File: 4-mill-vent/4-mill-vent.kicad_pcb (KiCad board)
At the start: 2 copper layers, 76.2 x 47.6 mm, 70 parts, among them J1 Fan, J2 Buzzer, J3 Power, J4 ICSP, Q3 PZT3904, Q4 PZT3904, Q5 TSM480P06CP, Q6 MMBT3904, SW1 Power_off, SW2 Power_On, SW3 Fan_Down, SW4 Fan_Up, U1 LM321, U2 ATmega328P-AU, U3 TPSM84212EAB, U4 LM1117-5.0, Y1 16.000MHZ

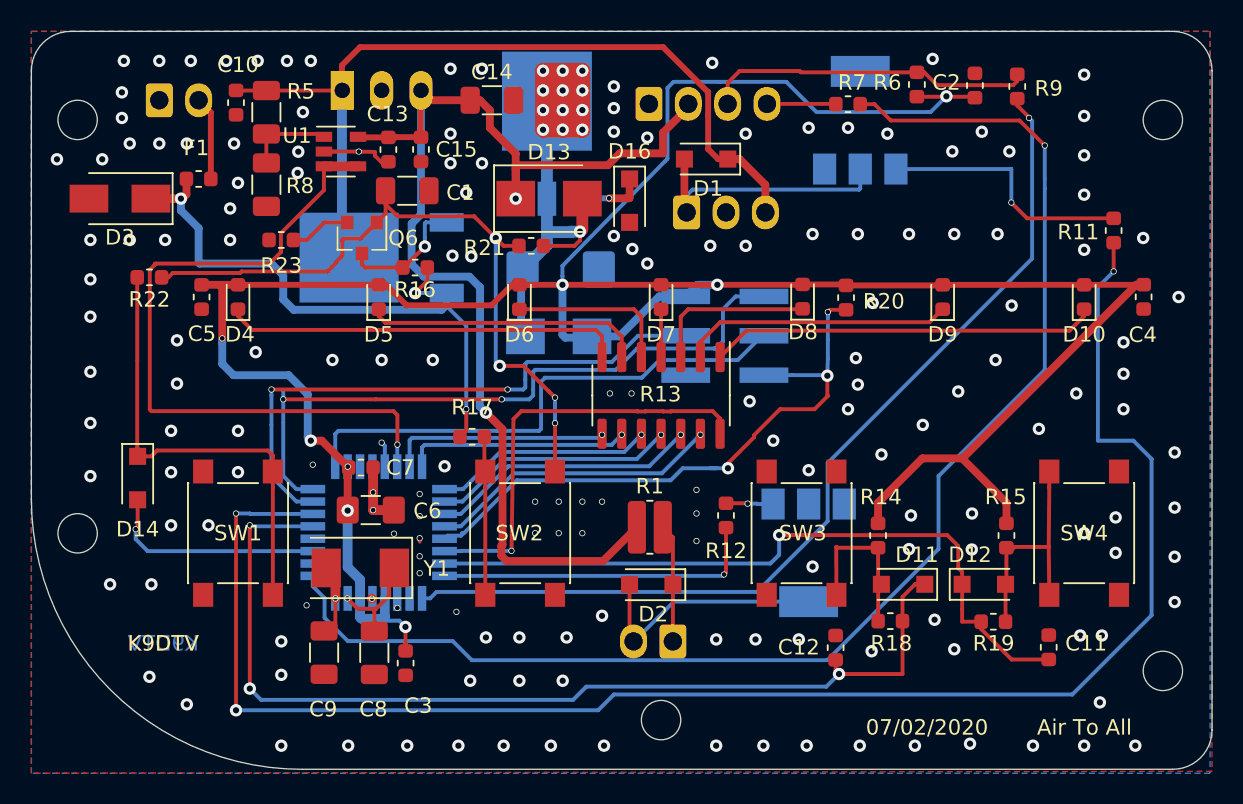
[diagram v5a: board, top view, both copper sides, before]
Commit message: a push so zip matches 4-mill folder
found a bad error, all fixed now
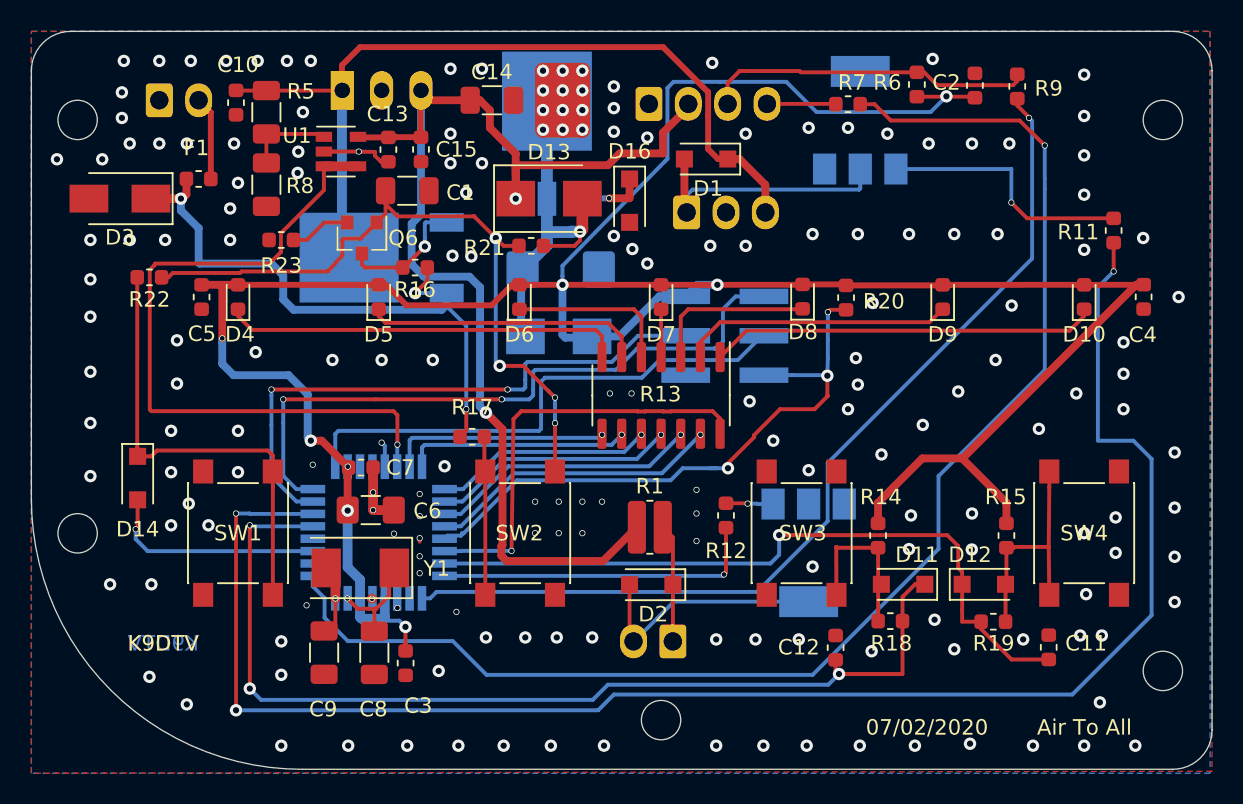
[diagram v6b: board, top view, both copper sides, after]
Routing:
- net PWM: track 88.6 -> 89.4 mm
- net MOSO: track 43.6 -> 43.1 mm
- net GND: vias 174 -> 175
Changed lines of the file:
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@@
     (thickness 1.6)
     (drawings 39)
-    (tracks 888)
+    (tracks 889)
     (zones 0)
     (modules 70)
@@
   )
   (setup
-    (last_trace_width 0.254)
+    (last_trace_width 0.25)
     (user_trace_width 0.254)
     (user_trace_width 0.381)
@@
   (via (at 121.1683 104.9443) (size 0.4) (drill 0.3) (layers F.Cu B.Cu) (net 2))
   (segment (start 121.1658 104.9418) (end 121.1683 104.9443) (width 0.635) (layer F.Cu) (net 2))
-  (via (at 130.683 107.442) (size 0.8) (drill 0.4) (layers F.Cu B.Cu) (net 2))
-  (via (at 127.508 110.236) (size 0.8) (drill 0.4) (layers F.Cu B.Cu) (net 2))
+  (via (at 131.064 107.442) (size 0.8) (drill 0.4) (layers F.Cu B.Cu) (net 2))
+  (via (at 125.476 109.601) (size 0.8) (drill 0.4) (layers F.Cu B.Cu) (net 2))
   (via (at 143.383 107.569) (size 0.8) (drill 0.4) (layers F.Cu B.Cu) (net 2))
   (via (at 148.717 107.569) (size 0.8) (drill 0.4) (layers F.Cu B.Cu) (net 2))
@@
   (via (at 138.938 83.312) (size 0.8) (drill 0.4) (layers F.Cu B.Cu) (net 2))
   (via (at 128.524 107.442) (size 0.8) (drill 0.4) (layers F.Cu B.Cu) (net 2))
-  (via (at 136.017 106.045) (size 0.8) (drill 0.4) (layers F.Cu B.Cu) (net 2))
-  (via (at 133.731 107.442) (size 0.8) (drill 0.4) (layers F.Cu B.Cu) (net 2))
-  (via (at 130.683 110.236) (size 0.8) (drill 0.4) (layers F.Cu B.Cu) (net 2))
+  (via (at 135.382 107.442) (size 0.8) (drill 0.4) (layers F.Cu B.Cu) (net 2))
+  (via (at 133.096 107.442) (size 0.8) (drill 0.4) (layers F.Cu B.Cu) (net 2))
   (via (at 149.606 102.87) (size 0.8) (drill 0.4) (layers F.Cu B.Cu) (net 2))
   (via (at 157.353 70.104) (size 0.8) (drill 0.4) (layers F.Cu B.Cu) (net 2))
@@
   (via (at 166.624 91.694) (size 0.8) (drill 0.4) (layers F.Cu B.Cu) (net 2))
   (via (at 164.211 93.98) (size 0.8) (drill 0.4) (layers F.Cu B.Cu) (net 2))
-  (via (at 158.623 76.073) (size 0.8) (drill 0.4) (layers F.Cu B.Cu) (net 2))
-  (via (at 162.306 76.073) (size 0.8) (drill 0.4) (layers F.Cu B.Cu) (net 2))
-  (via (at 160.528 74.803) (size 0.8) (drill 0.4) (layers F.Cu B.Cu) (net 2))
+  (via (at 157.099 75.565) (size 0.8) (drill 0.4) (layers F.Cu B.Cu) (net 2))
+  (via (at 162.306 75.565) (size 0.8) (drill 0.4) (layers F.Cu B.Cu) (net 2))
+  (via (at 159.893 75.565) (size 0.8) (drill 0.4) (layers F.Cu B.Cu) (net 2))
   (via (at 161.544 81.407) (size 0.8) (drill 0.4) (layers F.Cu B.Cu) (net 2))
   (via (at 155.829 81.407) (size 0.8) (drill 0.4) (layers F.Cu B.Cu) (net 2))
@@
   (via (at 133.223 100.711) (size 0.4) (drill 0.3) (layers F.Cu B.Cu) (net 2))
   (via (at 134.747 100.711) (size 0.4) (drill 0.3) (layers F.Cu B.Cu) (net 2))
-  (via (at 133.477 110.236) (size 0.8) (drill 0.4) (layers F.Cu B.Cu) (net 2))
+  (via (at 163.195 107.569) (size 0.8) (drill 0.4) (layers F.Cu B.Cu) (net 2))
+  (via (at 167.259 104.648) (size 0.8) (drill 0.4) (layers F.Cu B.Cu) (net 2))
+  (via (at 109.347 98.806) (size 0.8) (drill 0.4) (layers F.Cu B.Cu) (net 2))
   (via (at 113.284 100.203) (size 0.4) (drill 0.3) (layers F.Cu B.Cu) (net 3))
   (segment (start 113.3503 100.2693) (end 113.284 100.203) (width 0.25) (layer B.Cu) (net 3))
@@
   (segment (start 113.284 110.744) (end 113.284 100.485842) (width 0.25) (layer F.Cu) (net 3))
   (via (at 113.284 110.744) (size 0.8) (drill 0.4) (layers F.Cu B.Cu) (net 3))
-  (segment (start 114.011001 111.471001) (end 134.146999 111.471001) (width 0.254) (layer B.Cu) (net 3))
-  (segment (start 113.284 110.744) (end 114.011001 111.471001) (width 0.254) (layer B.Cu) (net 3))
-  (segment (start 134.146999 111.471001) (end 135.001 110.617) (width 0.254) (layer B.Cu) (net 3))
   (segment (start 155.4101 109.800826) (end 151.311174 109.800826) (width 0.254) (layer F.Cu) (net 3))
   (segment (start 151.0919 109.581552) (end 151.0919 108.89) (width 0.254) (layer F.Cu) (net 3))
@@
   (segment (start 151.311174 109.800826) (end 151.311174 109.800826) (width 0.254) (layer F.Cu) (net 3))
   (via (at 151.311174 109.800826) (size 0.8) (drill 0.4) (layers F.Cu B.Cu) (net 3))
-  (segment (start 150.495 110.617) (end 151.311174 109.800826) (width 0.254) (layer B.Cu) (net 3))
-  (segment (start 135.001 110.617) (end 150.495 110.617) (width 0.254) (layer B.Cu) (net 3))
+  (segment (start 136.398 110.49) (end 150.622 110.49) (width 0.254) (layer B.Cu) (net 3))
+  (segment (start 113.284 110.744) (end 114.011001 111.471001) (width 0.254) (layer B.Cu) (net 3))
+  (segment (start 150.622 110.49) (end 151.311174 109.800826) (width 0.254) (layer B.Cu) (net 3))
+  (segment (start 135.416999 111.471001) (end 136.398 110.49) (width 0.254) (layer B.Cu) (net 3))
+  (segment (start 114.011001 111.471001) (end 135.416999 111.471001) (width 0.254) (layer B.Cu) (net 3))
   (segment (start 160.4845 106.901) (end 160.4845 106.426) (width 0.254) (layer F.Cu) (net 4))
   (segment (start 162.448 108.8645) (end 160.4845 106.901) (width 0.254) (layer F.Cu) (net 4))
@@
   (segment (start 107.149686 83.39899) (end 106.82999 83.718686) (width 0.254) (layer F.Cu) (net 12))
   (segment (start 117.3483 104.1403) (end 117.3483 103.4693) (width 0.254) (layer B.Cu) (net 13))
-  (segment (start 127.618499 108.909101) (end 150.551899 108.909101) (width 0.25) (layer B.Cu) (net 13))
   (segment (start 118.11 104.902) (end 117.3483 104.1403) (width 0.254) (layer B.Cu) (net 13))
   (segment (start 118.11 106.172) (end 118.11 104.902) (width 0.254) (layer B.Cu) (net 13))
   (segment (start 126.385199 107.675801) (end 119.613801 107.675801) (width 0.254) (layer B.Cu) (net 13))
-  (segment (start 157.734 101.727) (end 157.734 97.028) (width 0.25) (layer B.Cu) (net 13))
-  (segment (start 126.385199 107.675801) (end 127.618499 108.909101) (width 0.25) (layer B.Cu) (net 13))
-  (segment (start 150.551899 108.909101) (end 157.734 101.727) (width 0.25) (layer B.Cu) (net 13))
-  (segment (start 157.734 97.028) (end 164.592 90.17) (width 0.25) (layer B.Cu) (net 13))
   (segment (start 119.613801 107.675801) (end 118.11 106.172) (width 0.254) (layer B.Cu) (net 13))
   (via (at 164.592 75.692) (size 0.4) (drill 0.3) (layers F.Cu B.Cu) (net 13))
@@
   (segment (start 164.592 78.486) (end 164.592 77.851) (width 0.25) (layer B.Cu) (net 13))
   (segment (start 164.592 90.17) (end 164.592 78.486) (width 0.25) (layer B.Cu) (net 13))
+  (segment (start 149.606 109.855) (end 157.734 101.727) (width 0.25) (layer B.Cu) (net 13))
+  (segment (start 128.564398 109.855) (end 149.606 109.855) (width 0.25) (layer B.Cu) (net 13))
+  (segment (start 157.734 101.727) (end 157.734 97.028) (width 0.25) (layer B.Cu) (net 13))
+  (segment (start 126.385199 107.675801) (end 128.564398 109.855) (width 0.25) (layer B.Cu) (net 13))
+  (segment (start 157.734 97.028) (end 164.592 90.17) (width 0.25) (layer B.Cu) (net 13))
   (segment (start 126.01256 85.26206) (end 125.971 85.2205) (width 0.762) (layer B.Cu) (net 14))
   (via (at 108.839 79.121) (size 0.8) (drill 0.4) (layers F.Cu B.Cu) (net 14))
@@
   (segment (start 115.443 97.014) (end 115.443 93.599) (width 0.25) (layer B.Cu) (net 46))
   (via (at 115.443 92.075) (size 0.4) (drill 0.3) (layers F.Cu B.Cu) (net 46))
-  (segment (start 115.443 93.599) (end 115.443 91.567) (width 0.254) (layer B.Cu) (net 46))
   (segment (start 143.275002 88.773) (end 143.252001 88.796001) (width 0.25) (layer B.Cu) (net 46))
   (segment (start 146.467 85.431) (end 144.642 85.431) (width 0.25) (layer B.Cu) (net 46))
@@
   (segment (start 131.318 92.075) (end 129.54 92.075) (width 0.254) (layer B.Cu) (net 46))
   (segment (start 131.572 91.821) (end 131.318 92.075) (width 0.254) (layer B.Cu) (net 46))
+  (segment (start 115.443 93.599) (end 115.443 92.075) (width 0.25) (layer B.Cu) (net 46))
   (via (at 119.5783 104.9243) (size 0.4) (drill 0.3) (layers F.Cu B.Cu) (net 47))
   (segment (start 122.6143 102.9553) (end 122.6143 103.0823) (width 0.635) (layer F.Cu) (net 47))

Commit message: And update was missed some where along the way and a reset cap was not added to the board
updated both zip and 4-mill-vent files so they are in sync.

cleaned up so grounds for the micro as well
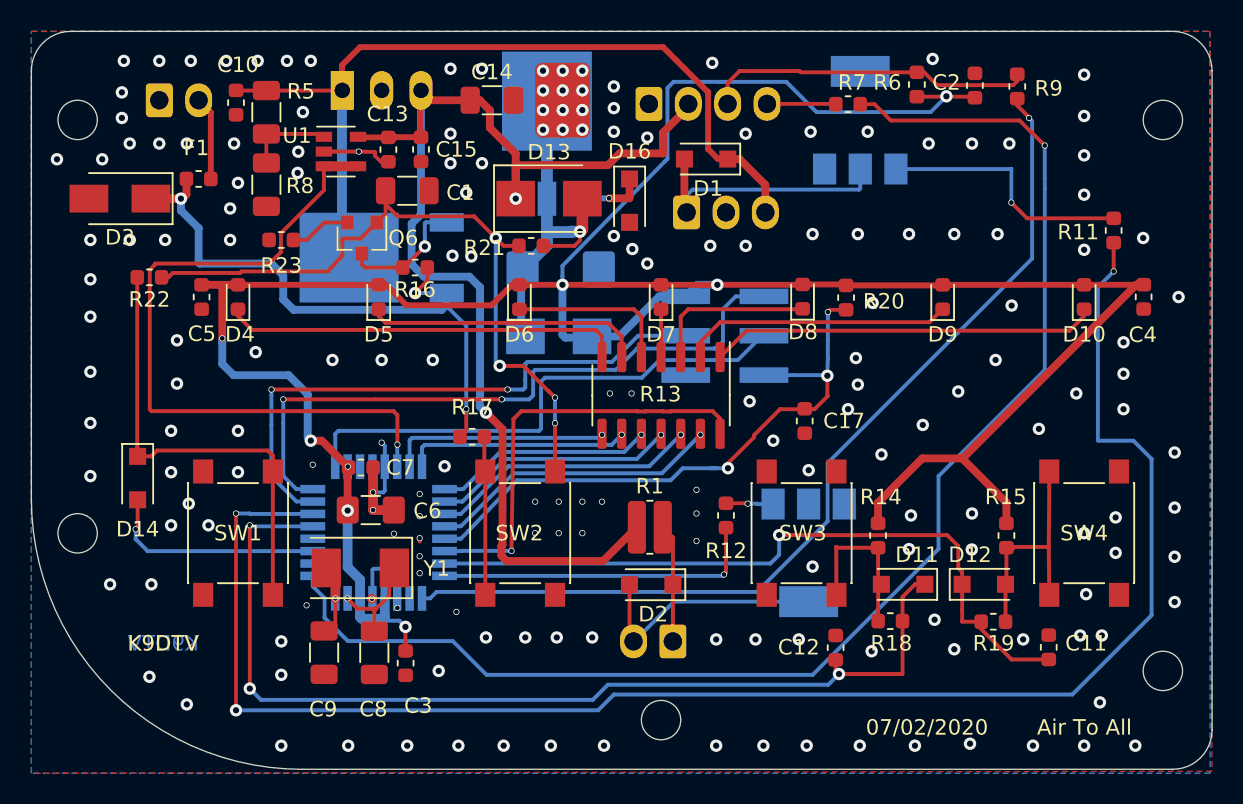
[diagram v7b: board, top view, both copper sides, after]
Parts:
- added C17: C0603C104M4RACTU, Capacitor_SMD:C_0603_1608Metric, F.Cu at (149.1, 93.5)
- R9: value 4.7k -> 1k
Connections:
- net Micro_power_Down renamed Net-(U2-Pad2)
- net PWM renamed Net-(R7-Pad1)
- net RPM renamed Net-(R9-Pad2)
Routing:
- net GND: track 11.3 -> 19.1 mm, vias 175 -> 174
- net +5V: track 224.6 -> 227.5 mm
